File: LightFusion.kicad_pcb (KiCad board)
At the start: 4 copper layers, 61 x 42 mm, 102 parts, among them J1 303C-C4115-30-04, J2 TC2030-IDC-FP, P1 PHR-2, U1 MDBT42-512KV2, U10 OPA381AIDGKR, U2 TPS7A2033PDBVR, U3 TPS22918DBVR, U4 DRV8837DSGR, U5 ADS1292IPBSR, U8 TMP1075NDRLR, U9 MCP3561T-E_ST

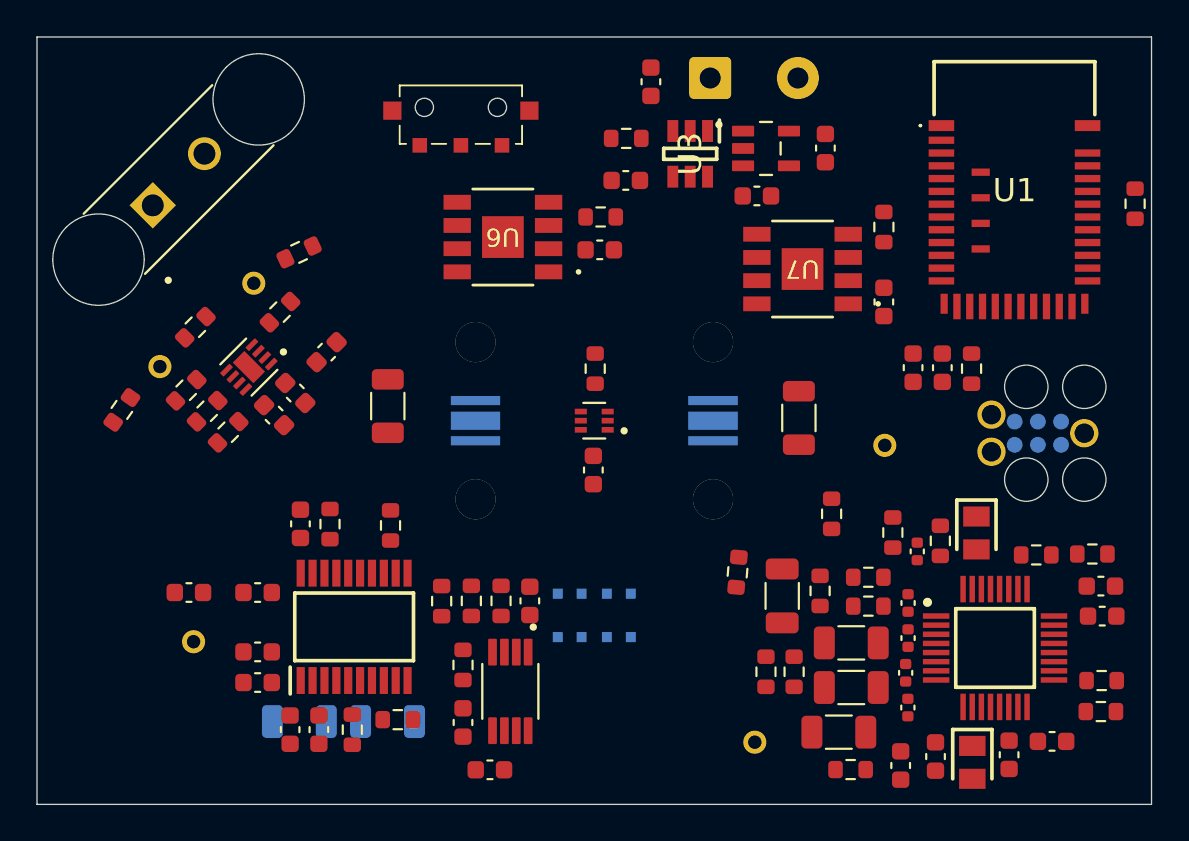
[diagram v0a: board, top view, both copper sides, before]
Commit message: rectangle placement before routing
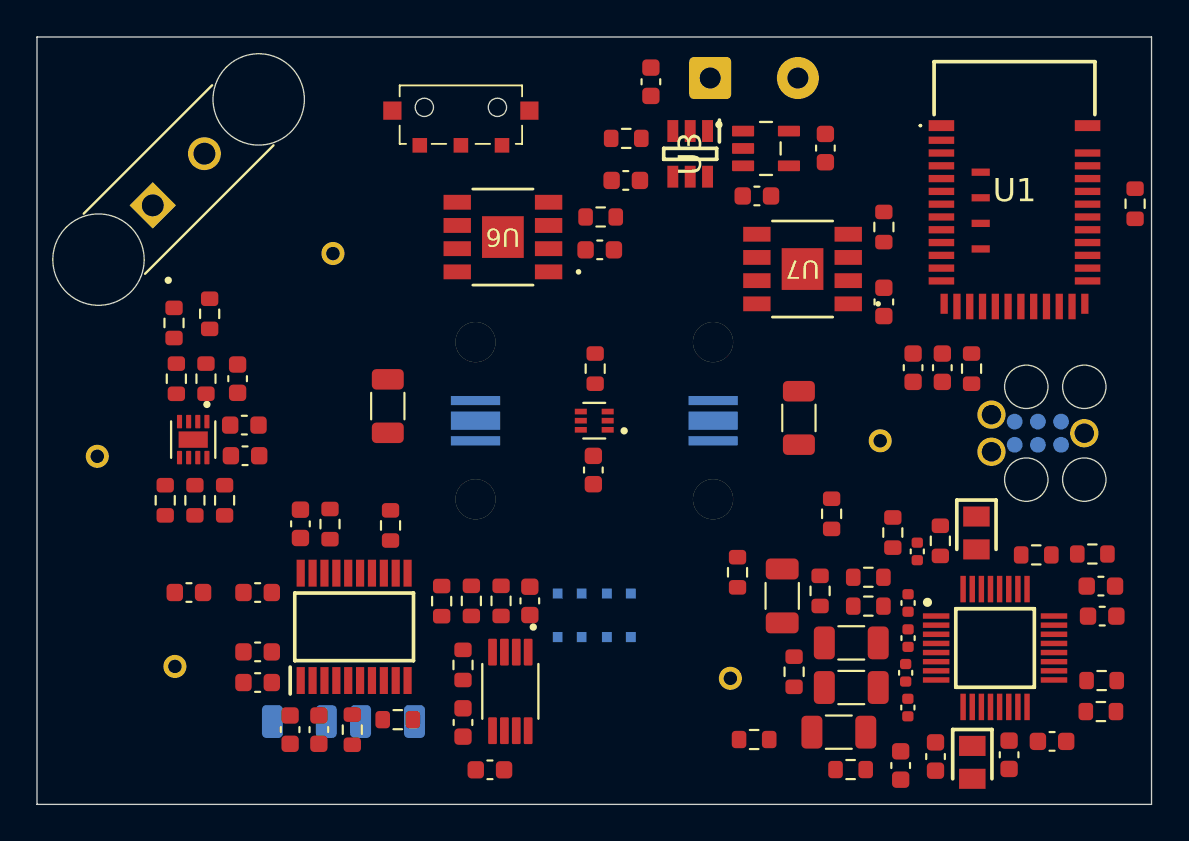
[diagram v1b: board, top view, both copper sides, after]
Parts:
- moved E4 12.8 mm to (122.8, 102.0), turned to 90 degrees
- moved E5 11.3 mm to (135.7, 90.8), turned to 180 degrees
- moved R23 7.86 mm to (127.0, 94.7), turned to 90 degrees
- moved R22 7.12 mm to (128.9, 94.2), turned to 90 degrees
- moved R20 6.74 mm to (127.1, 97.7), turned to 90 degrees
- moved R19 6.13 mm to (126.5, 104.4), turned to -90 degrees
- moved C21 5.08 mm to (130.5, 97.7), turned to 90 degrees
- moved U4 5.00 mm to (128.1, 101.0), turned to -90 degrees
- moved R18 4.92 mm to (128.1, 104.4), turned to -90 degrees
- moved R13 3.77 mm to (158.8, 117.5), turned to 0 degrees
- moved E1 3.74 mm to (157.4, 114.1)
- moved R17 3.73 mm to (129.8, 104.4), turned to 90 degrees
- moved C22 3.30 mm to (130.8, 100.2), turned to 0 degrees
- moved R21 2.88 mm to (128.7, 97.7), turned to 90 degrees
- moved C20 2.73 mm to (130.9, 101.9), turned to 0 degrees
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
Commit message: signal routed
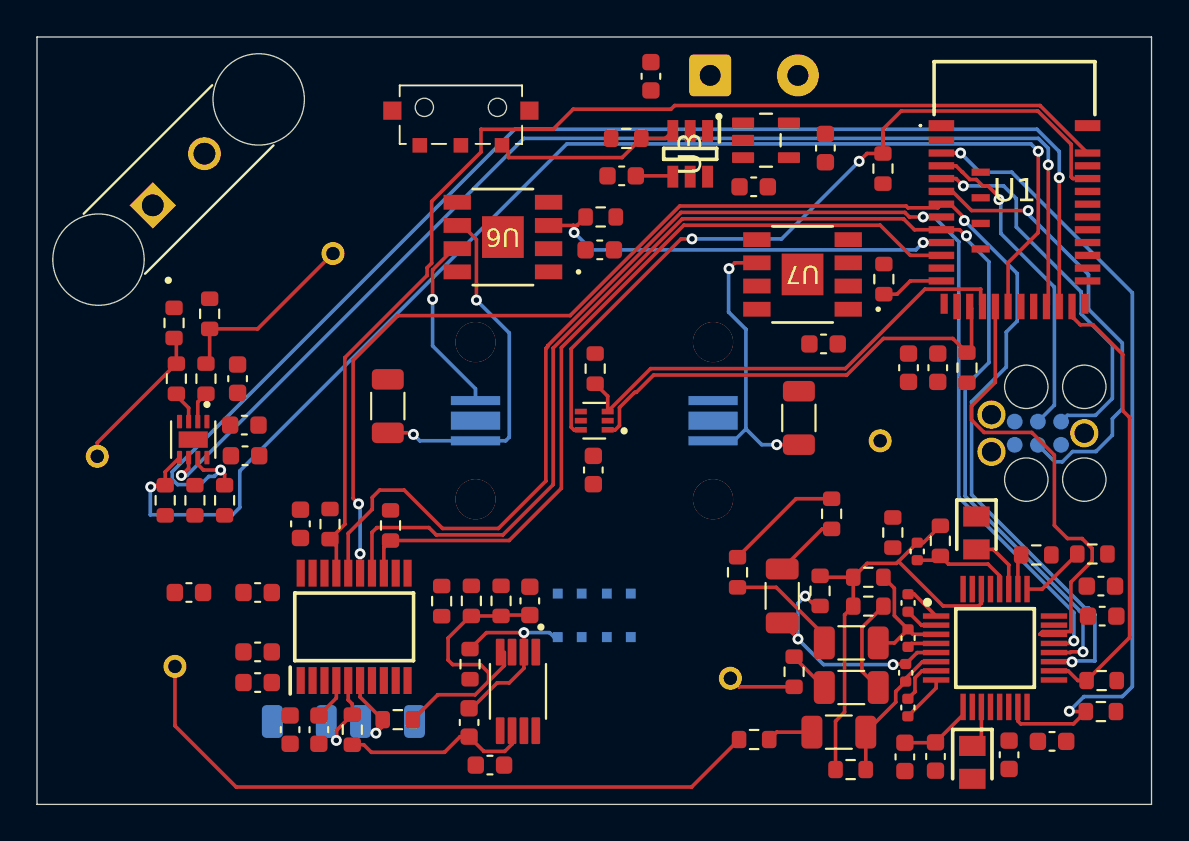
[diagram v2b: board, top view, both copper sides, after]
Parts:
- moved R2 13.9 mm to (165.8, 86.2)
- moved C29 4.02 mm to (162.6, 95.8), turned to 180 degrees
- moved R36 2.85 mm to (165.8, 92.2)
- moved C28 0.53 mm to (158.7, 87.2)
- moved C13 0.52 mm to (167.0, 118.4)
- moved U2 0.45 mm to (159.4, 84.7)
- moved U10 0.42 mm to (145.8, 114.8)
- moved R34 0.39 mm to (143.2, 113.3)
- moved C25 0.34 mm to (151.5, 86.6)
- moved C42 0.33 mm to (143.2, 116.5)
- moved C23 0.30 mm to (153.1, 81.2)
- moved U7 0.30 mm to (161.4, 92.0)
- moved C43 0.26 mm to (144.3, 118.8)
- moved R1 0.25 mm to (170.4, 97.1)
- moved C18 0.25 mm to (168.8, 97.1)
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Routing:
- net ADC_MOSI: track 0.00 -> 80.9 mm, vias 0 -> 4
- net ADC_MISO: track 0.00 -> 76.5 mm, vias 0 -> 2
- net ADC_SCK: track 0.00 -> 75.1 mm, vias 0 -> 2
- net /MCU_STIM_IN2: track 0.00 -> 71.8 mm, vias 0 -> 2
- net /MCU_STIM_EN: track 0.00 -> 71.5 mm, vias 0 -> 2
- net /MCU_STIM_IN1: track 0.00 -> 65.2 mm, vias 0 -> 2
- net ADC_DRDY_N: track 0.00 -> 62.7 mm
- net /EEG_RESET_N: track 0.00 -> 44.9 mm, vias 0 -> 2
- net ADC_CS_N: track 0.00 -> 44.4 mm
- net I2C_TEMP_SDA: track 0.00 -> 43.0 mm, vias 0 -> 2
- net Net-(E2-Pad1): track 0.00 -> 36.6 mm
- net /EEG_DRDY: track 0.00 -> 26.1 mm
- net TEMP_ALERT: track 0.00 -> 26.0 mm
- net I2C_TEMP_SCL: track 0.00 -> 25.3 mm
- net /EEG_CS_N: track 0.00 -> 25.2 mm
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
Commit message: ground routed
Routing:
- net GND: track 0.00 -> 122.4 mm, vias 0 -> 61
- net /MCU_STIM_IN2: track 71.8 -> 72.8 mm
- net /MCU_STIM_IN1: track 65.2 -> 66.2 mm
- net /MCU_STIM_EN: track 71.5 -> 72.4 mm
- net /PD_ADC/PHOTO_BIAS: track 16.1 -> 16.8 mm
- added copper zone on In1.Cu, net GND

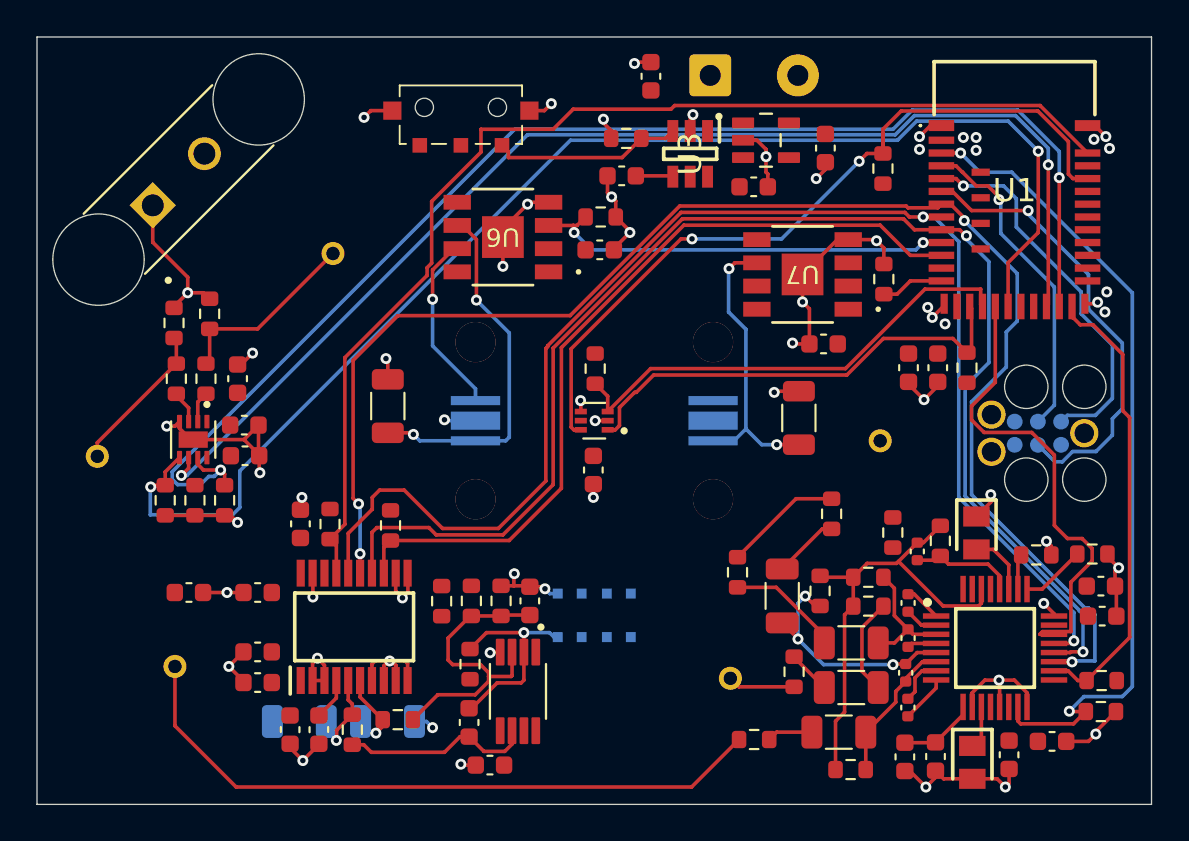
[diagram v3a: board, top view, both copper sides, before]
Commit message: routed 4 layers
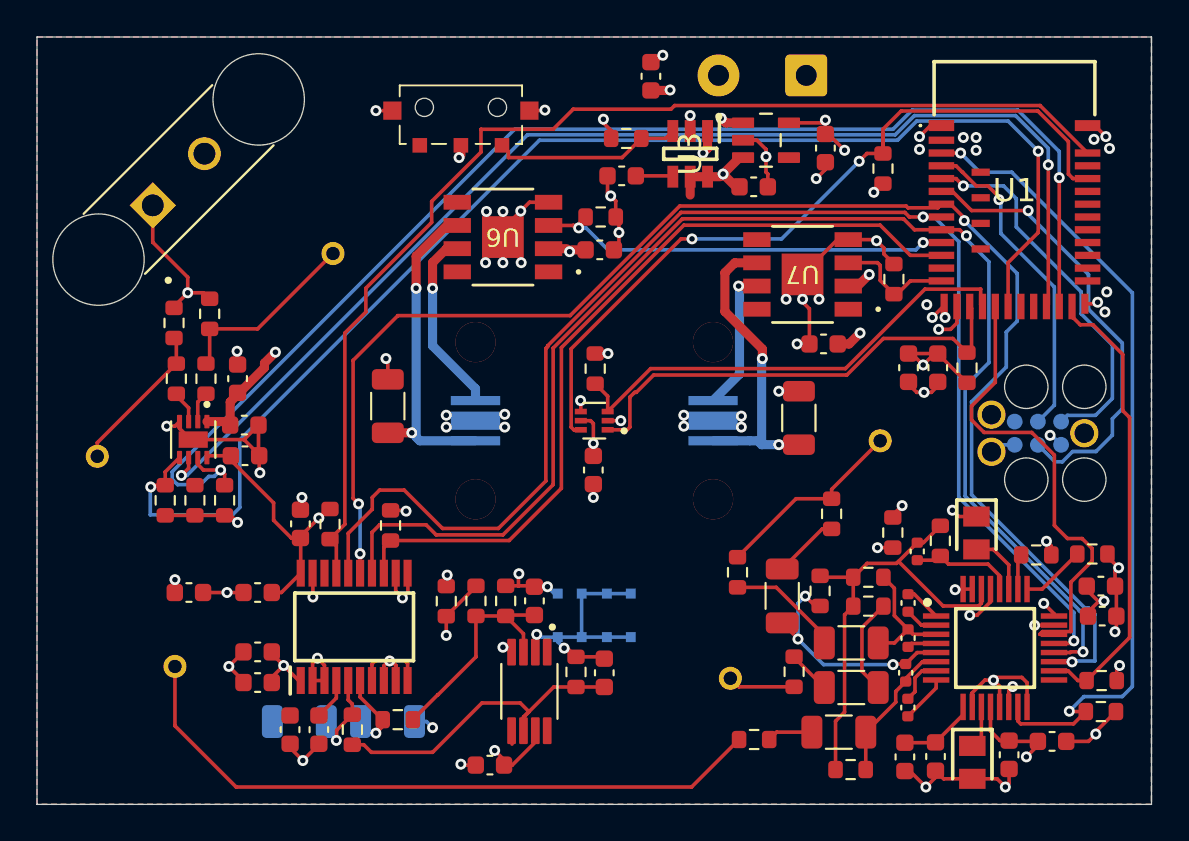
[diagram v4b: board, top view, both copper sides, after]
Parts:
- moved C42 7.88 mm to (150.6, 113.8)
- moved R34 5.82 mm to (149.0, 113.8)
- moved P1 5.25 mm to (161.6, 81.1), turned to 180 degrees
- moved U10 0.63 mm to (146.4, 114.8)
- moved R36 0.55 mm to (166.4, 92.2)
- moved R32 0.25 mm to (145.2, 109.9)
- moved R33 0.25 mm to (143.5, 109.9)
- moved C41 0.25 mm to (146.7, 109.9)
- moved R35 0.25 mm to (141.9, 109.9)
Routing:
- net 3V3_DIG: track 0.00 -> 134.6 mm, vias 0 -> 16
- net VBAT_SYSTEM: track 0.00 -> 86.8 mm, vias 0 -> 8
- net /Power/BAT+: track 0.00 -> 47.2 mm, vias 0 -> 2
- net /PD_ADC/3V3_A: track 0.00 -> 33.0 mm, vias 0 -> 3
- net /3V3_EEG_A: track 0.00 -> 25.2 mm, vias 0 -> 4
- net GND: track 122.4 -> 133.9 mm, vias 61 -> 75
- net Net-(D2-A): track 0.00 -> 7.89 mm, vias 0 -> 1
- net /PD_ADC/PHOTO_OUT: track 10.5 -> 17.4 mm
- net Net-(E3-Pad1): track 6.48 -> 10.7 mm
- net /PD_ADC/PHOTO_BIAS: track 16.8 -> 12.7 mm
- net PWM_850: track 3.45 -> 6.60 mm
- net /PD_ADC/PHOTO_TIA_IN: track 11.9 -> 14.5 mm, vias 1 -> 2
- net Net-(D1-K): track 19.8 -> 17.8 mm
- net /MCU_STIM_IN2: track 72.8 -> 73.8 mm
- net Net-(D2-K): track 16.3 -> 17.2 mm
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- added copper zone on B.Cu, net GND
- added copper zone on F.Cu, net GND
- added copper zone on In2.Cu, net GND

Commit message: routing finsihed, only few warnings left in DRC
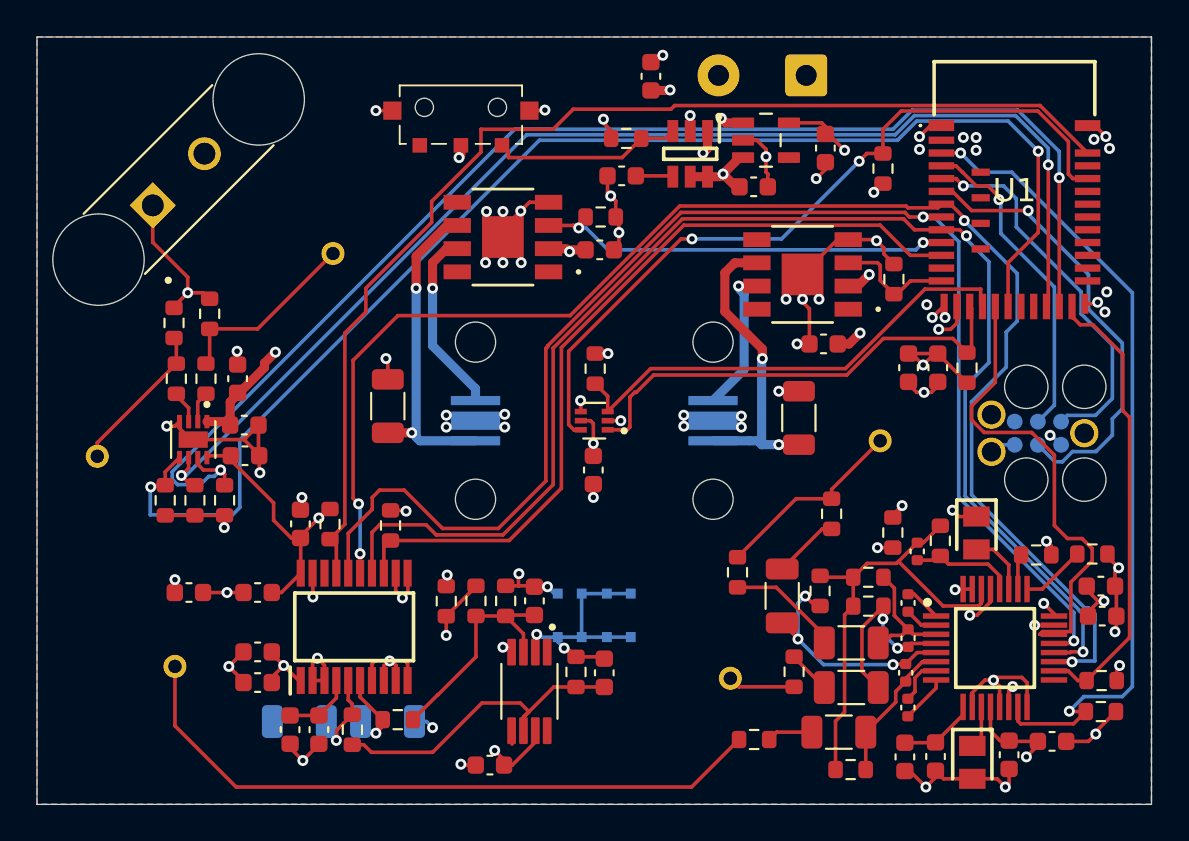
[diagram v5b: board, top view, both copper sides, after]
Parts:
- removed OPT1, OPT2: FP11055_LISA2-RS-PIN, LightFusion:LEDIL_FP11055_LISA2_RS_PIN
- added Ref**: Val**, LightFusion:LEDIL_FP11055_LISA2_RS_PIN, F.Cu at (156.5, 100.0)
- added Ref**: Val**, LightFusion:LEDIL_FP11055_LISA2_RS_PIN, F.Cu at (143.5, 100.0)
- U10: value OPA381AIDGKR -> SOP65P490X110-8N
- U2: value TPS7A2033PDBVR -> SOT95P280X145-5N
- U4: value DRV8837DSGR -> SON50P200X200X80-9N
- U5: value ADS1292IPBSR -> QFP50P700X700X120-32N
- U8: value TMP1075NDRLR -> SOT50P160X60-6N
- U9: value MCP3561T-E_ST -> SOP65P640X120-20N
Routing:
- net Net-(U5-IN1P): track 6.93 -> 10.2 mm, vias 0 -> 2
- net /PD_ADC/ADC_VREF: track 2.31 -> 3.88 mm
- net VBAT_SYSTEM: track 86.8 -> 85.8 mm
- net I2C_TEMP_SDA: track 43.0 -> 42.0 mm
- net /MCU_STIM_IN1: track 66.2 -> 67.2 mm
- net 3V3_DIG: track 134.6 -> 134.2 mm, vias 16 -> 15

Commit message: routing ready DRC passed
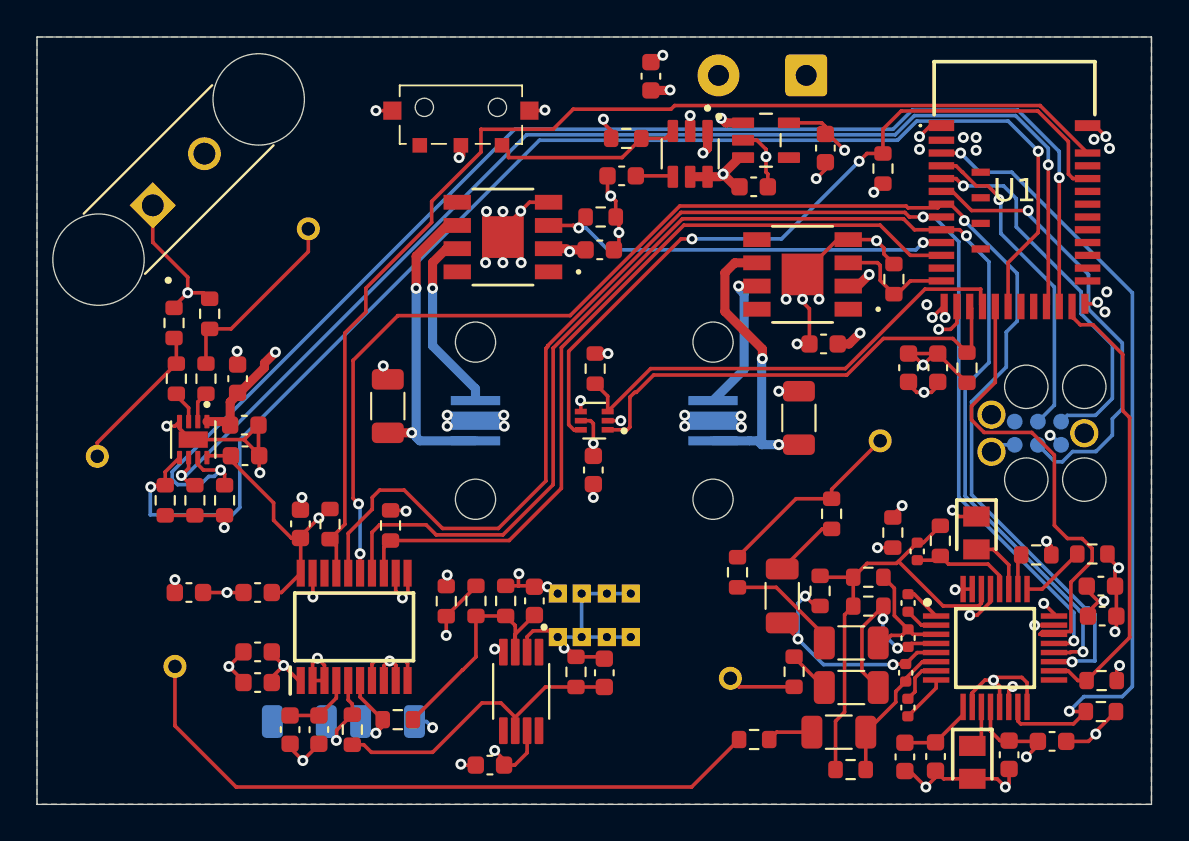
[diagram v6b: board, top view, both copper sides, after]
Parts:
- removed Ref** (x2): Val**, LightFusion:LEDIL_FP11055_LISA2_RS_PIN
- added OPT1: FP11055_LISA2-RS-PIN, LightFusion:LEDIL_FP11055_LISA2_RS_PIN, F.Cu at (143.5, 100.0)
- added OPT2: FP11055_LISA2-RS-PIN, LightFusion:LEDIL_FP11055_LISA2_RS_PIN, F.Cu at (156.5, 100.0)
- D3: footprint LightFusion:VEMD8082 -> LightFusion:VEMD8082_New
- U10: value SOP65P490X110-8N -> OPA381AIDGKR
- U2: value SOT95P280X145-5N -> TPS7A2033PDBVR
- U3: footprint LightFusion:TPS22918DBVT -> LightFusion:TPS22918DBVR-6N
- U4: value SON50P200X200X80-9N -> DRV8837DSGR
- U5: value QFP50P700X700X120-32N -> ADS1292IPBSR
- U8: value SOT50P160X60-6N -> TMP1075NDRLR
- U9: value SOP65P640X120-20N -> MCP3561T-E_ST
- moved E5 1.91 mm to (134.3, 89.5)
- moved U10 0.45 mm to (146.0, 114.8)
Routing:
- net GND: track 133.7 -> 120.7 mm
- net unconnected-(U10-Pad5): track 0.73 -> 0.00 mm
- net /PD_ADC/PHOTO_BIAS: track 12.7 -> 13.4 mm
- net /PD_ADC/PHOTO_OUT: track 17.4 -> 16.8 mm
- net /PD_ADC/PHOTO_TIA_IN: track 14.5 -> 15.1 mm, vias 2 -> 1
